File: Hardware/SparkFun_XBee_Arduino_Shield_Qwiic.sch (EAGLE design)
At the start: 75 parts, among them J4 QWIIC_RIGHT_ANGLE, Q1 220mA/50V/3.5Ω, Q3 3.1A/30V/105mΩ, Q5 20V/4.2A/52mΩ/1.4W, U1 FSUSB42MUX, U2 AP63203, U3 ESD Diode, U4 FT231XS, U5 ESD Diode, X1 JUMPER-SMT_2_NO_SILK

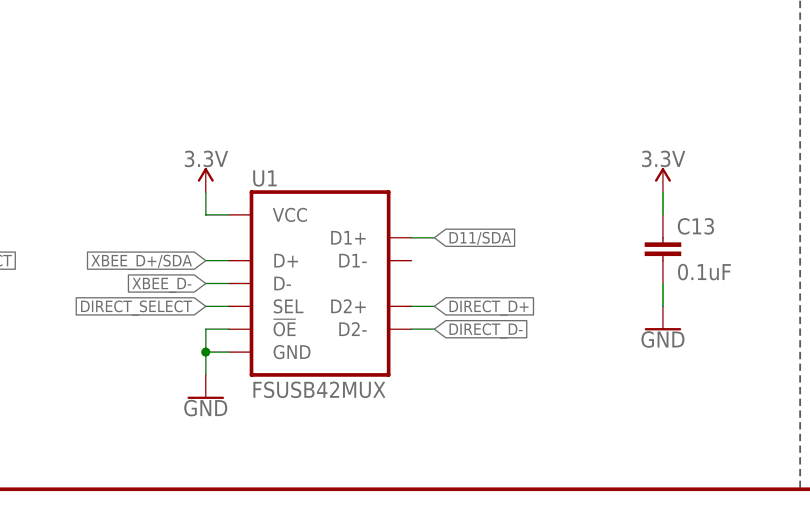
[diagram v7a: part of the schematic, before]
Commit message: Small adjustment to design file after approving proximity DRC error
* Remakes panels
* Deletes old library
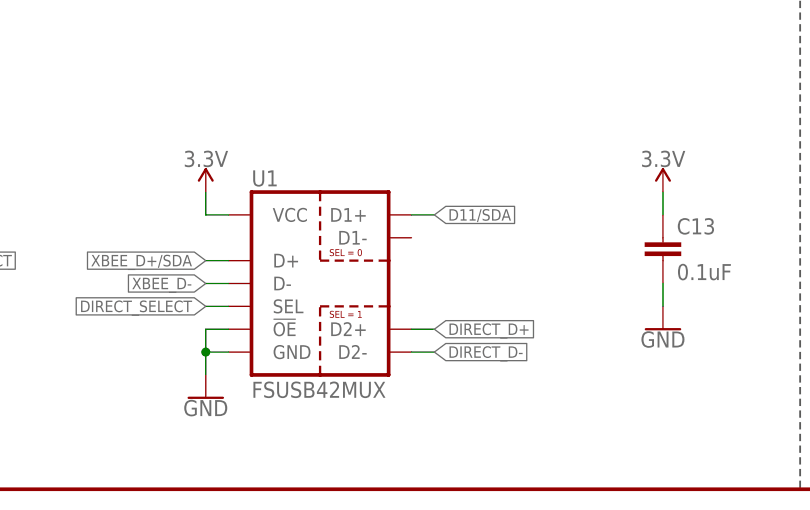
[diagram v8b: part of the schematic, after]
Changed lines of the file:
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@@
 </plain>
 <instances>
-<instance part="J4" gate="G$1" x="393.7" y="180.34" smashed="yes">
+<instance part="J4" gate="J1" x="393.7" y="180.34" smashed="yes">
 <attribute name="VALUE" x="373.38" y="175.006" size="1.778" layer="96" font="vector" align="top-left"/>
 <attribute name="NAME" x="388.62" y="188.214" size="1.778" layer="95" font="vector"/>
@@
 <net name="D11/SDA" class="0">
 <segment>
-<pinref part="J4" gate="G$1" pin="3"/>
+<pinref part="J4" gate="J1" pin="3"/>
 <wire x1="401.32" y1="182.88" x2="406.4" y2="182.88" width="0.1524" layer="91"/>
 <label x="406.4" y="182.88" size="1.27" layer="95" font="vector" xref="yes"/>
@@
 </segment>
 <segment>
-<wire x1="96.52" y1="27.94" x2="93.98" y2="27.94" width="0.1524" layer="91"/>
-<label x="96.52" y="27.94" size="1.27" layer="95" font="vector" xref="yes"/>
+<wire x1="96.52" y1="30.48" x2="93.98" y2="30.48" width="0.1524" layer="91"/>
+<label x="96.52" y="30.48" size="1.27" layer="95" font="vector" xref="yes"/>
 <pinref part="U1" gate="G$1" pin="D1+"/>
 </segment>
@@
 </segment>
 <segment>
-<pinref part="J4" gate="G$1" pin="4"/>
+<pinref part="J4" gate="J1" pin="4"/>
 <wire x1="401.32" y1="185.42" x2="406.4" y2="185.42" width="0.1524" layer="91"/>
 <label x="406.4" y="185.42" size="1.27" layer="95" font="vector" xref="yes"/>
@@
 <net name="GND" class="0">
 <segment>
-<pinref part="J4" gate="G$1" pin="1"/>
+<pinref part="J4" gate="J1" pin="1"/>
 <wire x1="401.32" y1="177.8" x2="403.86" y2="177.8" width="0.1524" layer="91"/>
 <wire x1="403.86" y1="177.8" x2="403.86" y2="175.26" width="0.1524" layer="91"/>
@@
 </segment>
 <segment>
-<pinref part="J4" gate="G$1" pin="2"/>
+<pinref part="J4" gate="J1" pin="2"/>
 <wire x1="403.86" y1="180.34" x2="401.32" y2="180.34" width="0.1524" layer="91"/>
 <pinref part="SUPPLY4" gate="G$1" pin="3.3V"/>
@@
 <net name="DIRECT_D+" class="2">
 <segment>
-<wire x1="96.52" y1="20.32" x2="93.98" y2="20.32" width="0.1524" layer="91"/>
-<label x="96.52" y="20.32" size="1.27" layer="95" font="vector" xref="yes"/>
+<wire x1="96.52" y1="17.78" x2="93.98" y2="17.78" width="0.1524" layer="91"/>
+<label x="96.52" y="17.78" size="1.27" layer="95" font="vector" xref="yes"/>
 <pinref part="U1" gate="G$1" pin="D2+"/>
 </segment>
@@
 <net name="DIRECT_D-" class="2">
 <segment>
-<wire x1="96.52" y1="17.78" x2="93.98" y2="17.78" width="0.1524" layer="91"/>
-<label x="96.52" y="17.78" size="1.27" layer="95" font="vector" xref="yes"/>
+<wire x1="96.52" y1="15.24" x2="93.98" y2="15.24" width="0.1524" layer="91"/>
+<label x="96.52" y="15.24" size="1.27" layer="95" font="vector" xref="yes"/>
 <pinref part="U1" gate="G$1" pin="D2-"/>
 </segment>
